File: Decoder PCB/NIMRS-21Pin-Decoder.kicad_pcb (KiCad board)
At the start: 4 copper layers, 30 x 23.5 mm, 93 parts, among them J1 21Pin Loco Socket, J2 U.FL, Q1 MMDT3904, Q2 MMDT3904, U1 ESP32-S3FN8, U2 MAX98357A, U4 DRV8213DSGR, U60 TPS63070, U70 TPS63070, X1 40Mhz

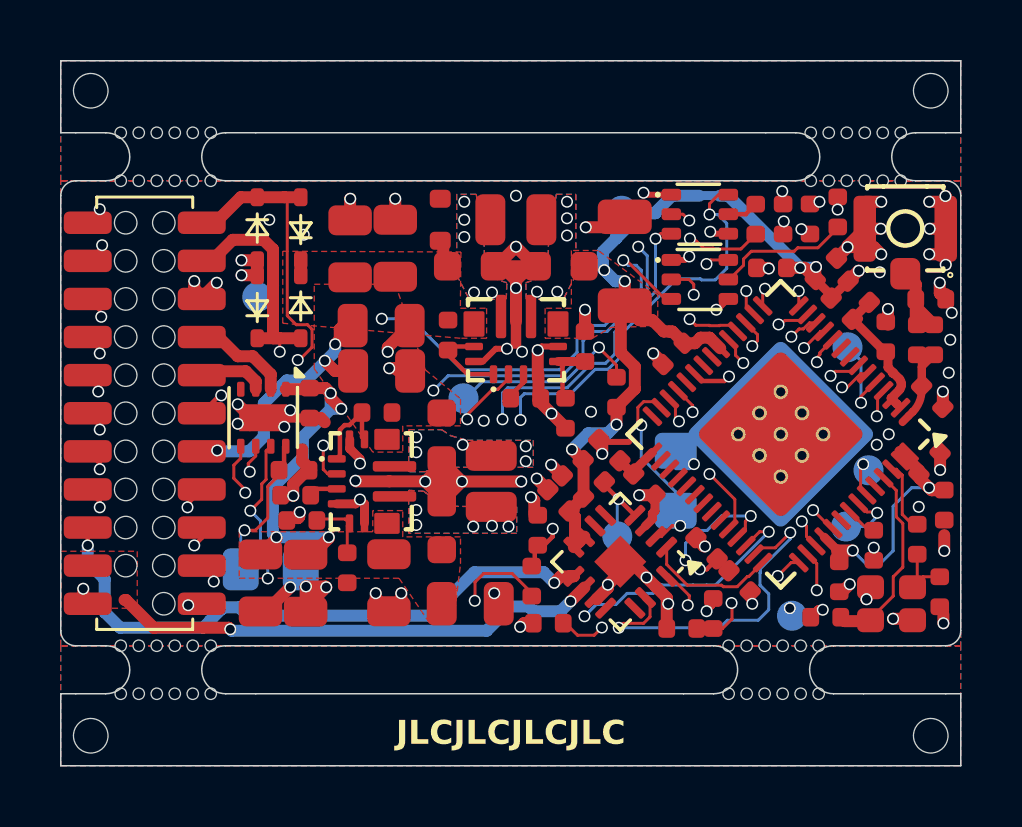
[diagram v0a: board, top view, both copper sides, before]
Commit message: Add alternative 21-pin socket
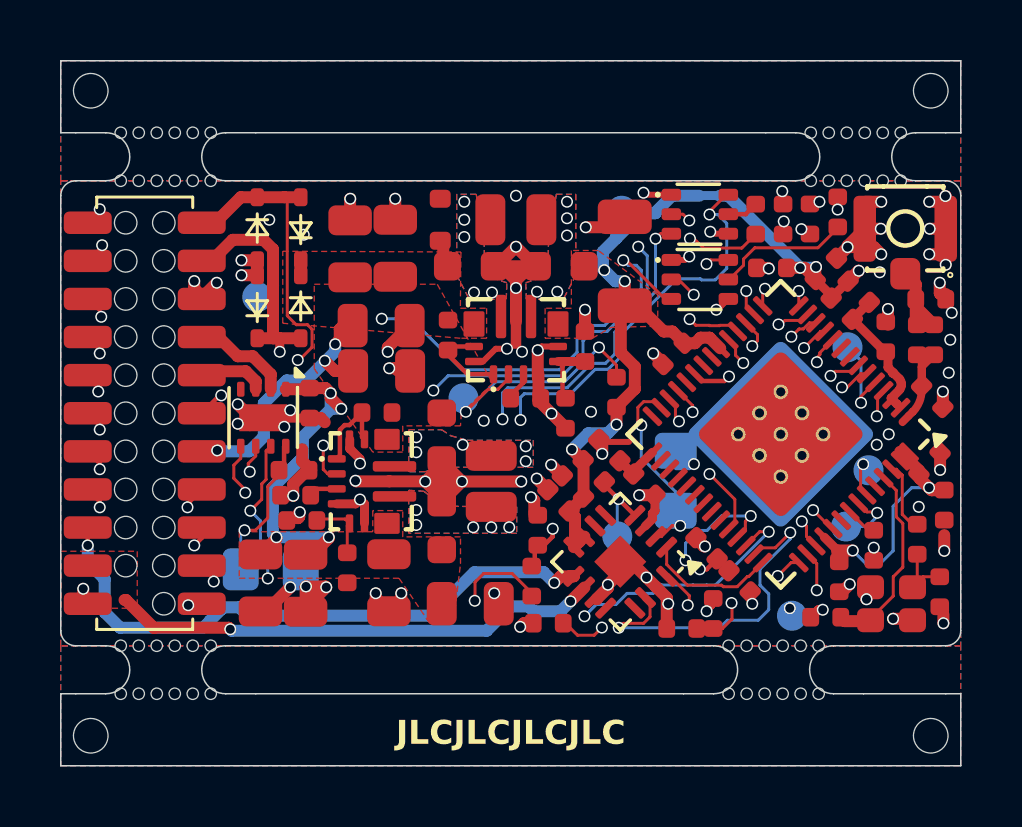
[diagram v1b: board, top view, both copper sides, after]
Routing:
- net /3V3_PG/ESP_EN: track 25.8 -> 21.7 mm
- net /AUX5: track 26.7 -> 26.1 mm

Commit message: Add extra test points
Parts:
- removed C4: 10uF, PCM_JLCPCB:C_0402
- removed C5, C6: 1uF, PCM_JLCPCB:C_0402
- removed L2, L4, L5: 3.9nH,300mA, PCM_JLCPCB:L_0402
- added TP10: Test Point, Custom_Footprints:TestPoint_Pad_D1.0mm, B.Cu at (143.3, 104.8)
- added TP9: Test Point, Custom_Footprints:TestPoint_Pad_D1.0mm, B.Cu at (143.2, 102.7)
- C1, C11, C16, C2, C7, C9: value 100nF -> 10uF
- C17: value 100nF -> 1uF
- C75: value 10nF -> 10uF
- L1: value 3.9nH,300mA -> 2.7nH
- moved TP6 6.90 mm to (143.8, 107.2)
- moved L1 2.91 mm to (162.7, 102.7), turned to 90 degrees
- moved R13 2.21 mm to (158.5, 100.0), turned to 180 degrees
- moved C2 1.79 mm to (160.6, 101.6), turned to 90 degrees
- moved L3 0.27 mm to (162.8, 109.1)
- moved C13 0.14 mm to (162.9, 101.3)
- moved R14 0.08 mm to (158.1, 98.6)
- moved R15 0.08 mm to (157.2, 98.6)
- moved R12 0.08 mm to (159.0, 98.6)
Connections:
- C1 pad 1: Net-(C1-Pad1) -> +3V3
- L1 pad 1: +3V3 -> /LNA_IN
- L1 pad 2: Net-(C1-Pad1) -> /LNA_OUT
- U1 pad 2: Net-(C1-Pad1) -> +3V3
- U1 pad 3: Net-(C1-Pad1) -> +3V3
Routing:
- net GND: track 77.5 -> 72.7 mm, vias 79 -> 78
- net Net-(C1-Pad1): track 4.53 -> 0.00 mm
- net /AUX2: track 5.91 -> 2.19 mm, vias 2 -> 0
- net Net-(Q1B-B2): track 4.51 -> 1.97 mm
- net /AUX1: track 6.36 -> 3.86 mm, vias 2 -> 0
- net /LNA_OUT: track 2.96 -> 1.98 mm
- net /LNA_IN: track 3.70 -> 2.92 mm
- net /VDD_SPI (OUTPUT): track 1.63 -> 1.00 mm
- net /REAR: track 7.50 -> 8.12 mm
- net +3V3: track 97.9 -> 97.5 mm, vias 12 -> 8
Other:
- board text added: "NIMRS Decoder V0.1.0"
- board text added: "VCC"
- board text added: "VMOTOR"
